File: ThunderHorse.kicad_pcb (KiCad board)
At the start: 2 copper layers, 0 parts

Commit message: Initial layout
Added the components to the board.

TODO:
Review the schematic before continuing the layout.
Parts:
- added BZ1: Buzzer, Custom_Parts:FUET_9018, F.Cu at (226.4, 77.0)
- added C1: 10u, Capacitor_SMD:C_0805_2012Metric, F.Cu at (266.6, 53.8)
- added C10: 10u, Capacitor_SMD:C_0805_2012Metric, F.Cu at (266.6, 62.8)
- added C100: 1u, Capacitor_SMD:C_0603_1608Metric, F.Cu at (263.8, 120.0)
- added C101: 10u, Capacitor_SMD:C_0805_2012Metric, F.Cu at (238.9, 68.2)
- added C11: 10u, Capacitor_SMD:C_0805_2012Metric, F.Cu at (266.6, 65.8)
- added C12: 22u, Capacitor_SMD:C_1206_3216Metric, F.Cu at (261.5, 70.7)
- added C13: 22u, Capacitor_SMD:C_1206_3216Metric, F.Cu at (261.5, 74.0)
- added C14: 10u, Capacitor_SMD:C_0805_2012Metric, F.Cu at (266.6, 68.8)
- added C15: 22u, Capacitor_SMD:C_1206_3216Metric, F.Cu at (261.5, 77.4)
- added C16: 15p, Capacitor_SMD:C_0603_1608Metric, F.Cu at (222.6, 52.9)
- added C17: 100n, Capacitor_SMD:C_0603_1608Metric, F.Cu at (222.6, 55.4)
- added C18: 10u, Capacitor_SMD:C_0805_2012Metric, F.Cu at (238.9, 53.2)
- added C19: 100n, Capacitor_SMD:C_0603_1608Metric, F.Cu at (222.6, 57.9)
- added C2: 10u, Capacitor_SMD:C_0805_2012Metric, F.Cu at (266.6, 56.8)
- added C20: 15p, Capacitor_SMD:C_0603_1608Metric, F.Cu at (222.6, 60.5)
- added C21: 100n, Capacitor_SMD:C_0603_1608Metric, F.Cu at (222.6, 63.0)
- added C22: 100n, Capacitor_SMD:C_0603_1608Metric, F.Cu at (222.6, 65.5)
- added C23: 100n, Capacitor_SMD:C_0603_1608Metric, F.Cu at (222.6, 68.0)
- added C24: 100n, Capacitor_SMD:C_0603_1608Metric, F.Cu at (222.6, 70.5)
- added C25: 100n, Capacitor_SMD:C_0603_1608Metric, F.Cu at (226.6, 52.9)
- added C26: 10u, Capacitor_SMD:C_0805_2012Metric, F.Cu at (238.9, 56.2)
- added C27: 100n, Capacitor_SMD:C_0603_1608Metric, F.Cu at (226.6, 55.4)
- added C28: 100n, Capacitor_SMD:C_0603_1608Metric, F.Cu at (226.6, 57.9)
- added C29: 100n, Capacitor_SMD:C_0603_1608Metric, F.Cu at (226.6, 60.5)
- added C3: 10u, Capacitor_SMD:C_0805_2012Metric, F.Cu at (266.6, 59.8)
- added C30: 10u, Capacitor_SMD:C_0805_2012Metric, F.Cu at (238.9, 59.2)
- added C31: 100n, Capacitor_SMD:C_0603_1608Metric, F.Cu at (226.6, 63.0)
- added C32: 100n, Capacitor_SMD:C_0603_1608Metric, F.Cu at (226.6, 65.5)
- added C33: 10u, Capacitor_SMD:C_0805_2012Metric, F.Cu at (238.9, 62.2)
- added C34: 100n, Capacitor_SMD:C_0805_2012Metric, F.Cu at (238.9, 65.2)
- added C35: 1u, Capacitor_SMD:C_0603_1608Metric, F.Cu at (174.4, 18.5)
- added C36: 10u, Capacitor_SMD:C_1206_3216Metric, F.Cu at (187.2, 18.9)
- added C37: 100n, Capacitor_SMD:C_0603_1608Metric, F.Cu at (174.4, 21.0)
- added C38: 10u, Capacitor_SMD:C_1206_3216Metric, F.Cu at (187.2, 22.2)
- added C39: 10u, Capacitor_SMD:C_1206_3216Metric, F.Cu at (187.2, 25.6)
- added C4: 22u, Capacitor_SMD:C_1206_3216Metric, F.Cu at (261.5, 54.0)
- added C40: 10u, Capacitor_SMD:C_1206_3216Metric, F.Cu at (187.2, 28.9)
- added C41: 10u, Capacitor_SMD:C_1206_3216Metric, F.Cu at (187.2, 32.3)
- added C42: 10u, Capacitor_SMD:C_0805_2012Metric, F.Cu at (192.3, 31.3)
- added C43: 1u, Capacitor_SMD:C_0603_1608Metric, F.Cu at (174.4, 23.5)
- added C44: 1u, Capacitor_SMD:C_0603_1608Metric, F.Cu at (174.4, 26.0)
- added C45: 1u, Capacitor_SMD:C_0603_1608Metric, F.Cu at (174.4, 28.5)
- added C46: 1u, Capacitor_SMD:C_0603_1608Metric, F.Cu at (202.3, 18.5)
- added C47: 10u, Capacitor_SMD:C_1206_3216Metric, F.Cu at (215.2, 18.9)
- added C48: 100n, Capacitor_SMD:C_0603_1608Metric, F.Cu at (202.3, 21.0)
- added C49: 10u, Capacitor_SMD:C_1206_3216Metric, F.Cu at (215.2, 22.2)
- added C5: 100n, Capacitor_SMD:C_0603_1608Metric, F.Cu at (270.8, 53.5)
- added C50: 10u, Capacitor_SMD:C_1206_3216Metric, F.Cu at (215.2, 25.6)
- added C51: 10u, Capacitor_SMD:C_1206_3216Metric, F.Cu at (215.2, 28.9)
- added C52: 10u, Capacitor_SMD:C_1206_3216Metric, F.Cu at (215.2, 32.3)
- added C53: 10u, Capacitor_SMD:C_0805_2012Metric, F.Cu at (220.2, 31.3)
- added C54: 1u, Capacitor_SMD:C_0603_1608Metric, F.Cu at (202.3, 23.5)
- added C55: 1u, Capacitor_SMD:C_0603_1608Metric, F.Cu at (202.3, 26.0)
- added C56: 1u, Capacitor_SMD:C_0603_1608Metric, F.Cu at (202.3, 28.5)
- added C57: 1u, Capacitor_SMD:C_0603_1608Metric, F.Cu at (257.8, 18.1)
- added C58: 10u, Capacitor_SMD:C_1206_3216Metric, F.Cu at (270.6, 18.5)
- added C59: 100n, Capacitor_SMD:C_0603_1608Metric, F.Cu at (257.8, 20.6)
- added C6: 22u, Capacitor_SMD:C_1206_3216Metric, F.Cu at (261.5, 57.3)
- added C60: 10u, Capacitor_SMD:C_1206_3216Metric, F.Cu at (270.6, 21.9)
- added C61: 10u, Capacitor_SMD:C_1206_3216Metric, F.Cu at (270.6, 25.2)
- added C62: 10u, Capacitor_SMD:C_1206_3216Metric, F.Cu at (270.6, 28.6)
- added C63: 10u, Capacitor_SMD:C_1206_3216Metric, F.Cu at (270.6, 31.9)
- added C64: 10u, Capacitor_SMD:C_0805_2012Metric, F.Cu at (275.7, 31.0)
- added C65: 1u, Capacitor_SMD:C_0603_1608Metric, F.Cu at (257.8, 23.1)
- added C66: 1u, Capacitor_SMD:C_0603_1608Metric, F.Cu at (257.8, 25.6)
- added C67: 1u, Capacitor_SMD:C_0603_1608Metric, F.Cu at (257.8, 28.1)
- added C68: 1u, Capacitor_SMD:C_0603_1608Metric, F.Cu at (230.2, 18.0)
- added C69: 10u, Capacitor_SMD:C_1206_3216Metric, F.Cu at (243.0, 18.4)
- added C7: 22u, Capacitor_SMD:C_1206_3216Metric, F.Cu at (261.5, 60.6)
- added C70: 100n, Capacitor_SMD:C_0603_1608Metric, F.Cu at (230.2, 20.5)
- added C71: 10u, Capacitor_SMD:C_1206_3216Metric, F.Cu at (243.0, 21.7)
- added C72: 10u, Capacitor_SMD:C_1206_3216Metric, F.Cu at (243.0, 25.1)
- added C73: 10u, Capacitor_SMD:C_1206_3216Metric, F.Cu at (243.0, 28.4)
- added C74: 10u, Capacitor_SMD:C_1206_3216Metric, F.Cu at (243.0, 31.8)
- added C75: 10u, Capacitor_SMD:C_0805_2012Metric, F.Cu at (248.1, 30.8)
- added C76: 1u, Capacitor_SMD:C_0603_1608Metric, F.Cu at (230.2, 23.0)
- added C77: 1u, Capacitor_SMD:C_0603_1608Metric, F.Cu at (230.2, 25.5)
- added C78: 1u, Capacitor_SMD:C_0603_1608Metric, F.Cu at (230.2, 28.0)
- added C79: 10u, Capacitor_SMD:C_0805_2012Metric, F.Cu at (238.4, 93.7)
- added C8: 22u, Capacitor_SMD:C_1206_3216Metric, F.Cu at (261.5, 64.0)
- added C80: 100n, Capacitor_SMD:C_0603_1608Metric, F.Cu at (250.7, 93.5)
- added C81: 10u, Capacitor_SMD:C_0805_2012Metric, F.Cu at (238.4, 96.8)
- added C82: 10u, Capacitor_SMD:C_0805_2012Metric, F.Cu at (238.4, 99.8)
- added C83: 100n, Capacitor_SMD:C_0201_0603Metric, F.Cu at (247.5, 93.1)
- added C84: 100n, Capacitor_SMD:C_0201_0603Metric, F.Cu at (247.5, 94.9)
- added C85: 100n, Capacitor_SMD:C_0201_0603Metric, F.Cu at (247.5, 96.6)
- added C86: 10u, Capacitor_SMD:C_0805_2012Metric, F.Cu at (272.0, 122.8)
- added C87: 10n, Capacitor_SMD:C_0603_1608Metric, F.Cu at (259.8, 112.5)
- added C88: 10n, Capacitor_SMD:C_0603_1608Metric, F.Cu at (259.8, 115.0)
- added C89: 10u, Capacitor_SMD:C_0805_2012Metric, F.Cu at (272.0, 125.8)
- added C9: 22u, Capacitor_SMD:C_1206_3216Metric, F.Cu at (261.5, 67.3)
- added C90: 100n, Capacitor_SMD:C_0603_1608Metric, F.Cu at (259.8, 117.5)
- added C91: 100n, Capacitor_SMD:C_0603_1608Metric, F.Cu at (259.8, 120.0)
- added C92: 100n, Capacitor_SMD:C_0603_1608Metric, F.Cu at (263.8, 112.5)
- added C94: 100p, Capacitor_SMD:C_0603_1608Metric, F.Cu at (263.8, 115.0)
- added C96: 100p, Capacitor_SMD:C_0603_1608Metric, F.Cu at (263.8, 117.5)
- added D1: 1N5819WS, Diode_SMD:D_SOD-323, F.Cu at (266.2, 100.7)
- added D2: WS2812B, Custom_Parts:WS2812B-2020, F.Cu at (234.3, 76.6)
- added D3: LED, LED_SMD:LED_0805_2012Metric, F.Cu at (234.4, 73.3)
- added FL1: LFB182G45SG9B740, Custom_Parts:LFB182G45SG9B740, F.Cu at (266.3, 129.1)
- added H1: M4, Custom_Parts:MOUNTING_FC_4.0mm, B.Cu at (162.0, 74.0)
- added H2: M4, Custom_Parts:MOUNTING_FC_4.0mm, B.Cu at (118.0, 126.0)
- added H3: M4, Custom_Parts:MOUNTING_FC_4.0mm, B.Cu at (162.0, 126.0)
- added H4: M4, Custom_Parts:MOUNTING_FC_4.0mm, B.Cu at (118.0, 74.0)
- added J1: JTAG, Custom_Parts:PAD_5_SQUARE_SOLID_1.0x1.0mm_P1.5mm, F.Cu at (245.3, 52.9)
- added J10: MOTOR2, Custom_Parts:PAD_3_SQUARE_SOLID_2.0x2.0mm_P2.5mm, F.Cu at (205.2, 36.7)
- added J11: SWD3, Custom_Parts:PAD_2_SQUARE_SOLID_1.0x1.0mm_P1.5mm, F.Cu at (257.8, 39.5)
- added J12: MOTOR3, Custom_Parts:PAD_3_SQUARE_SOLID_2.0x2.0mm_P2.5mm, F.Cu at (260.6, 36.3)
- added J13: SWD4, Custom_Parts:PAD_2_SQUARE_SOLID_1.0x1.0mm_P1.5mm, F.Cu at (230.1, 39.4)
- added J14: MOTOR4, Custom_Parts:PAD_3_SQUARE_SOLID_2.0x2.0mm_P2.5mm, F.Cu at (233.0, 36.2)
- added J16: UFL, Connector_Coaxial:U.FL_Hirose_U.FL-R-SMT-1_Vertical, F.Cu at (267.0, 124.3)
- added J2: HH-16P-CB-TYPE-C, Custom_Parts:HH-16P-CB-TYPE-C, F.Cu at (267.6, 90.3)
- added J3: GPS, Custom_Parts:PAD_6_SQUARE_SOLID_1.5x1.5mm_P2.0mm, F.Cu at (227.1, 93.6)
- added J4: CAM, Custom_Parts:PAD_6_SQUARE_SOLID_1.5x1.5mm_P2.0mm, F.Cu at (227.1, 96.7)
- added J5: GPS, Connector_JST:JST_SH_SM06B-SRSS-TB_1x06-1MP_P1.00mm_Horizontal, F.Cu at (226.0, 102.0)
- added J6: CAM, Connector_JST:JST_SH_SM06B-SRSS-TB_1x06-1MP_P1.00mm_Horizontal, F.Cu at (226.0, 109.6)
- added J7: SWD1, Custom_Parts:PAD_2_SQUARE_SOLID_1.0x1.0mm_P1.5mm, F.Cu at (174.3, 39.9)
- added J8: MOTOR1, Custom_Parts:PAD_3_SQUARE_SOLID_2.0x2.0mm_P2.5mm, F.Cu at (177.2, 36.7)
- added J9: SWD2, Custom_Parts:PAD_2_SQUARE_SOLID_1.0x1.0mm_P1.5mm, F.Cu at (202.3, 39.9)
- added L1: 1.5u, Inductor_SMD:L_Panasonic_PCC-M0530M, F.Cu at (273.2, 68.1)
- added L2: B201610S3R3, Custom_Parts:AOTAB201610S3R3101T, F.Cu at (249.4, 62.2)
- added L3: 15u, Inductor_SMD:L_0603_1608Metric, F.Cu at (267.8, 112.5)
- added Q1: SI2301BDS, Package_TO_SOT_SMD:SOT-23, F.Cu at (266.5, 97.0)
- added Q10: XRS306D, Custom_Parts:PDFN8_DUAL_3.3x3.3mm, F.Cu at (279.4, 37.1)
- added Q11: XRS306D, Custom_Parts:PDFN8_DUAL_3.3x3.3mm, F.Cu at (242.5, 37.0)
- added Q12: XRS306D, Custom_Parts:PDFN8_DUAL_3.3x3.3mm, F.Cu at (247.2, 37.0)
- added Q13: XRS306D, Custom_Parts:PDFN8_DUAL_3.3x3.3mm, F.Cu at (251.8, 37.0)
- added Q14: SI2312BDS, Package_TO_SOT_SMD:SOT-23, F.Cu at (249.2, 65.9)
- added Q2: XRS306D, Custom_Parts:PDFN8_DUAL_3.3x3.3mm, F.Cu at (186.7, 37.5)
- added Q3: XRS306D, Custom_Parts:PDFN8_DUAL_3.3x3.3mm, F.Cu at (191.4, 37.5)
- added Q4: XRS306D, Custom_Parts:PDFN8_DUAL_3.3x3.3mm, F.Cu at (196.0, 37.5)
- added Q5: XRS306D, Custom_Parts:PDFN8_DUAL_3.3x3.3mm, F.Cu at (214.7, 37.5)
- added Q6: XRS306D, Custom_Parts:PDFN8_DUAL_3.3x3.3mm, F.Cu at (219.3, 37.5)
- added Q7: XRS306D, Custom_Parts:PDFN8_DUAL_3.3x3.3mm, F.Cu at (224.0, 37.5)
- added Q8: XRS306D, Custom_Parts:PDFN8_DUAL_3.3x3.3mm, F.Cu at (270.1, 37.1)
- added Q9: XRS306D, Custom_Parts:PDFN8_DUAL_3.3x3.3mm, F.Cu at (274.8, 37.1)
- added R1: 10K, Resistor_SMD:R_0603_1608Metric, F.Cu at (270.8, 56.0)
- added R10: 27, Resistor_SMD:R_0603_1608Metric, F.Cu at (230.6, 60.5)
- added R11: 27, Resistor_SMD:R_0603_1608Metric, F.Cu at (230.6, 63.0)
- added R12: 1K, Resistor_SMD:R_0603_1608Metric, F.Cu at (230.6, 65.5)
- added R13: 5.1K, Resistor_SMD:R_0603_1608Metric, F.Cu at (230.6, 68.0)
- added R14: 5.1K, Resistor_SMD:R_0603_1608Metric, F.Cu at (230.6, 70.5)
- added R15: 10K, Resistor_SMD:R_0603_1608Metric, F.Cu at (234.6, 52.9)
- added R16: 5.1K, Resistor_SMD:R_0603_1608Metric, F.Cu at (262.1, 96.1)
- added R17: 5.1K, Resistor_SMD:R_0603_1608Metric, F.Cu at (262.1, 98.6)
- added R18: 10K, Resistor_SMD:R_0603_1608Metric, F.Cu at (262.1, 101.1)
- added R19: 10K, Resistor_SMD:R_0603_1608Metric, F.Cu at (174.4, 31.0)
- added R2: 680K, Resistor_SMD:R_0603_1608Metric, F.Cu at (270.8, 58.5)
- added R20: 10K, Resistor_SMD:R_0603_1608Metric, F.Cu at (174.4, 33.5)
- added R21: 2.2K, Resistor_SMD:R_0603_1608Metric, F.Cu at (178.4, 18.5)
- added R22: 10K, Resistor_SMD:R_0603_1608Metric, F.Cu at (178.4, 21.0)
- added R23: 1K, Resistor_SMD:R_0603_1608Metric, F.Cu at (178.4, 23.5)
- added R24: 10K, Resistor_SMD:R_0603_1608Metric, F.Cu at (178.4, 26.0)
- added R25: 2.2K, Resistor_SMD:R_0603_1608Metric, F.Cu at (178.4, 28.5)
- added R26: 10K, Resistor_SMD:R_0603_1608Metric, F.Cu at (178.4, 31.0)
- added R27: 10K, Resistor_SMD:R_0603_1608Metric, F.Cu at (178.4, 33.5)
- added R28: 2.2K, Resistor_SMD:R_0603_1608Metric, F.Cu at (182.4, 18.5)
- added R29: 10, Resistor_SMD:R_0603_1608Metric, F.Cu at (182.4, 21.0)
- added R3: 130K, Resistor_SMD:R_0603_1608Metric, F.Cu at (270.8, 61.1)
- added R30: 10, Resistor_SMD:R_0603_1608Metric, F.Cu at (182.4, 23.5)
- added R31: 10, Resistor_SMD:R_0603_1608Metric, F.Cu at (182.4, 26.0)
- added R32: 10, Resistor_SMD:R_0603_1608Metric, F.Cu at (182.4, 28.5)
- added R33: 10, Resistor_SMD:R_0603_1608Metric, F.Cu at (182.4, 31.0)
- added R34: 10, Resistor_SMD:R_0603_1608Metric, F.Cu at (182.4, 33.5)
- added R35: 10K, Resistor_SMD:R_0603_1608Metric, F.Cu at (202.3, 31.0)
- added R36: 10K, Resistor_SMD:R_0603_1608Metric, F.Cu at (202.3, 33.5)
- added R37: 2.2K, Resistor_SMD:R_0603_1608Metric, F.Cu at (206.3, 18.5)
- added R38: 10K, Resistor_SMD:R_0603_1608Metric, F.Cu at (206.3, 21.0)
- added R39: 1K, Resistor_SMD:R_0603_1608Metric, F.Cu at (206.3, 23.5)
- added R4: 100K, Resistor_SMD:R_0603_1608Metric, F.Cu at (270.8, 63.6)
- added R40: 10K, Resistor_SMD:R_0603_1608Metric, F.Cu at (206.3, 26.0)
- added R41: 2.2K, Resistor_SMD:R_0603_1608Metric, F.Cu at (206.3, 28.5)
- added R42: 10K, Resistor_SMD:R_0603_1608Metric, F.Cu at (206.3, 31.0)
- added R43: 10K, Resistor_SMD:R_0603_1608Metric, F.Cu at (206.3, 33.5)
- added R44: 2.2K, Resistor_SMD:R_0603_1608Metric, F.Cu at (210.4, 18.5)
- added R45: 10, Resistor_SMD:R_0603_1608Metric, F.Cu at (210.4, 21.0)
- added R46: 10, Resistor_SMD:R_0603_1608Metric, F.Cu at (210.4, 23.5)
- added R47: 10, Resistor_SMD:R_0603_1608Metric, F.Cu at (210.4, 26.0)
- added R48: 10, Resistor_SMD:R_0603_1608Metric, F.Cu at (210.4, 28.5)
- added R49: 10, Resistor_SMD:R_0603_1608Metric, F.Cu at (210.4, 31.0)
- added R5: 1K, Resistor_SMD:R_0603_1608Metric, F.Cu at (226.6, 68.0)
- added R50: 10, Resistor_SMD:R_0603_1608Metric, F.Cu at (210.4, 33.5)
- added R51: 10K, Resistor_SMD:R_0603_1608Metric, F.Cu at (257.8, 30.6)
- added R52: 10K, Resistor_SMD:R_0603_1608Metric, F.Cu at (257.8, 33.2)
- added R53: 2.2K, Resistor_SMD:R_0603_1608Metric, F.Cu at (261.8, 18.1)
- added R54: 10K, Resistor_SMD:R_0603_1608Metric, F.Cu at (261.8, 20.6)
- added R55: 1K, Resistor_SMD:R_0603_1608Metric, F.Cu at (261.8, 23.1)
- added R56: 10K, Resistor_SMD:R_0603_1608Metric, F.Cu at (261.8, 25.6)
- added R57: 2.2K, Resistor_SMD:R_0603_1608Metric, F.Cu at (261.8, 28.1)
- added R58: 10K, Resistor_SMD:R_0603_1608Metric, F.Cu at (261.8, 30.6)
- added R59: 10K, Resistor_SMD:R_0603_1608Metric, F.Cu at (261.8, 33.2)
- added R6: 10K, Resistor_SMD:R_0603_1608Metric, F.Cu at (226.6, 70.5)
- added R60: 2.2K, Resistor_SMD:R_0603_1608Metric, F.Cu at (265.8, 18.1)
- added R61: 10, Resistor_SMD:R_0603_1608Metric, F.Cu at (265.8, 20.6)
- added R62: 10, Resistor_SMD:R_0603_1608Metric, F.Cu at (265.8, 23.1)
- added R63: 10, Resistor_SMD:R_0603_1608Metric, F.Cu at (265.8, 25.6)
- added R64: 10, Resistor_SMD:R_0603_1608Metric, F.Cu at (265.8, 28.1)
- added R65: 10, Resistor_SMD:R_0603_1608Metric, F.Cu at (265.8, 30.6)
- added R66: 10, Resistor_SMD:R_0603_1608Metric, F.Cu at (265.8, 33.2)
- added R67: 10K, Resistor_SMD:R_0603_1608Metric, F.Cu at (230.2, 30.5)
- added R68: 10K, Resistor_SMD:R_0603_1608Metric, F.Cu at (230.2, 33.0)
- added R69: 2.2K, Resistor_SMD:R_0603_1608Metric, F.Cu at (234.2, 18.0)
- added R7: 100K, Resistor_SMD:R_0603_1608Metric, F.Cu at (230.6, 52.9)
- added R70: 10K, Resistor_SMD:R_0603_1608Metric, F.Cu at (234.2, 20.5)
- added R71: 1K, Resistor_SMD:R_0603_1608Metric, F.Cu at (234.2, 23.0)
- added R72: 10K, Resistor_SMD:R_0603_1608Metric, F.Cu at (234.2, 25.5)
- added R73: 2.2K, Resistor_SMD:R_0603_1608Metric, F.Cu at (234.2, 28.0)
- added R74: 10K, Resistor_SMD:R_0603_1608Metric, F.Cu at (234.2, 30.5)
- added R75: 10K, Resistor_SMD:R_0603_1608Metric, F.Cu at (234.2, 33.0)
- added R76: 2.2K, Resistor_SMD:R_0603_1608Metric, F.Cu at (238.2, 18.0)
- added R77: 10, Resistor_SMD:R_0603_1608Metric, F.Cu at (238.2, 20.5)
- added R78: 10, Resistor_SMD:R_0603_1608Metric, F.Cu at (238.2, 23.0)
- added R79: 10, Resistor_SMD:R_0603_1608Metric, F.Cu at (238.2, 25.5)
- added R8: 10K, Resistor_SMD:R_0603_1608Metric, F.Cu at (230.6, 55.4)
- added R80: 10, Resistor_SMD:R_0603_1608Metric, F.Cu at (238.2, 28.0)
- added R81: 10, Resistor_SMD:R_0603_1608Metric, F.Cu at (238.2, 30.5)
- added R82: 10, Resistor_SMD:R_0603_1608Metric, F.Cu at (238.2, 33.0)
- added R83: 10K, Resistor_SMD:R_0603_1608Metric, F.Cu at (250.7, 96.0)
- added R84: R002, Resistor_SMD:R_2512_6332Metric, F.Cu at (245.0, 100.0)
- added R85: 10K, Resistor_SMD:R_0603_1608Metric, F.Cu at (267.8, 115.0)
- added R86: 100K, Resistor_SMD:R_0603_1608Metric, F.Cu at (267.8, 117.5)
- added R87: 100K, Resistor_SMD:R_0603_1608Metric, F.Cu at (267.8, 120.0)
- added R88: 1K, Resistor_SMD:R_0603_1608Metric, F.Cu at (234.6, 55.4)
- added R89: 100, Resistor_SMD:R_0603_1608Metric, F.Cu at (234.6, 57.9)
- added R9: 27, Resistor_SMD:R_0603_1608Metric, F.Cu at (230.6, 57.9)
- added R90: 100K, Resistor_SMD:R_0603_1608Metric, F.Cu at (234.6, 60.5)
- added SW1: TS2306A, Custom_Parts:SW_SMD_3.0x2.0_PUSH, F.Cu at (243.9, 62.3)
- added SW2: TS2306A, Custom_Parts:SW_SMD_3.0x2.0_PUSH, F.Cu at (243.9, 65.5)
- added U1: 21700_DUAL_HOLDER, Custom_Parts:21700_DUAL_HOLDER_MOUNTING, B.Cu at (140.0, 100.0)
- added U10: DRV8300D, Custom_Parts:VQFN-24-1EP_4x4mm_P0.5mm_EP2.45x2.45mm, F.Cu at (221.2, 26.7)
- added U11: STM32G071GBUxN, Custom_Parts:QFN-28_4x4mm_P0.5mm, F.Cu at (277.0, 20.0)
- added U12: DRV8300D, Custom_Parts:VQFN-24-1EP_4x4mm_P0.5mm_EP2.45x2.45mm, F.Cu at (276.6, 26.3)
- added U13: STM32G071GBUxN, Custom_Parts:QFN-28_4x4mm_P0.5mm, F.Cu at (249.4, 19.9)
- added U14: DRV8300D, Custom_Parts:VQFN-24-1EP_4x4mm_P0.5mm_EP2.45x2.45mm, F.Cu at (249.0, 26.2)
- added U15: TPRT9013-33, Package_TO_SOT_SMD:SOT-23-5, F.Cu at (248.2, 104.9)
- added U16: ICM-42688-P, Custom_Parts:ICM-42688-P, F.Cu at (243.1, 104.8)
- added U17: BMP280, Package_LGA:Bosch_LGA-8_2x2.5mm_P0.65mm_ClockwisePinNumbering, F.Cu at (238.4, 103.3)
- added U18: INA230, Package_DFN_QFN:VQFN-16-1EP_3x3mm_P0.5mm_EP1.6x1.6mm_ThermalVias, F.Cu at (243.6, 94.9)
- added U19: TPRT9013-33, Package_TO_SOT_SMD:SOT-23-5, F.Cu at (272.4, 118.9)
- added U2: TPS63070RNMR, Custom_Parts:TPS63070RNMR, F.Cu at (275.5, 54.8)
- added U20: SX1280IMLTRT, Package_DFN_QFN:QFN-24-1EP_4x4mm_P0.5mm_EP2.6x2.6mm_ThermalVias, F.Cu at (261.3, 124.4)
- added U21: AT2401C, Package_DFN_QFN:QFN-16-1EP_3x3mm_P0.5mm_EP1.7x1.7mm_ThermalVias, F.Cu at (272.9, 113.9)
- added U3: TPRT9013-33, Package_TO_SOT_SMD:SOT-23-5, F.Cu at (271.4, 73.8)
- added U4: RP2354B, Custom_Parts:RP2350B_QFN-80_EP_10.573x10.573_Pitch0.4mm, F.Cu at (243.1, 76.2)
- added U5: W25Q128JVPIQ, Package_SON:WSON-8-1EP_6x5mm_P1.27mm_EP3.4x4.3mm, F.Cu at (245.3, 57.4)
- added U6: TPD2E001DRLR, Package_TO_SOT_SMD:SOT-553, F.Cu at (270.7, 96.5)
- added U7: STM32G071GBUxN, Custom_Parts:QFN-28_4x4mm_P0.5mm, F.Cu at (193.6, 20.4)
- added U8: DRV8300D, Custom_Parts:VQFN-24-1EP_4x4mm_P0.5mm_EP2.45x2.45mm, F.Cu at (193.2, 26.7)
- added U9: STM32G071GBUxN, Custom_Parts:QFN-28_4x4mm_P0.5mm, F.Cu at (221.5, 20.4)
- added Y1: 40MHz, Crystal:Crystal_SMD_2016-4Pin_2.0x1.6mm, F.Cu at (234.2, 80.2)
- added Y2: 52MHz/10ppm, Crystal:Crystal_SMD_2016-4Pin_2.0x1.6mm, F.Cu at (271.8, 129.1)
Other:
- board outline added: 120 x 60 mm

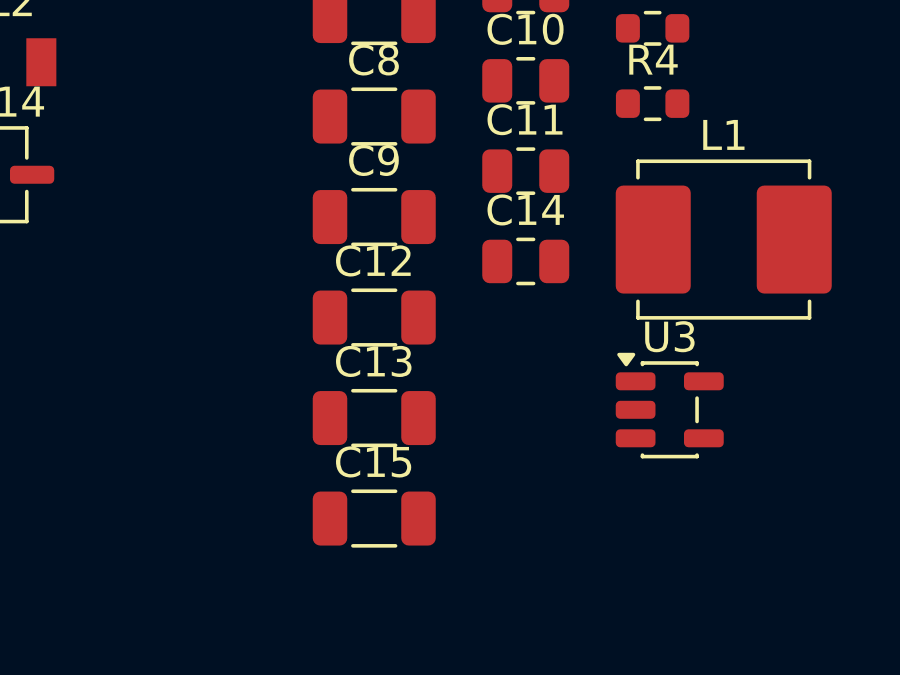
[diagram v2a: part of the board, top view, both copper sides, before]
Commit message: Net nodes
Added the missing net nodes in the schematic.
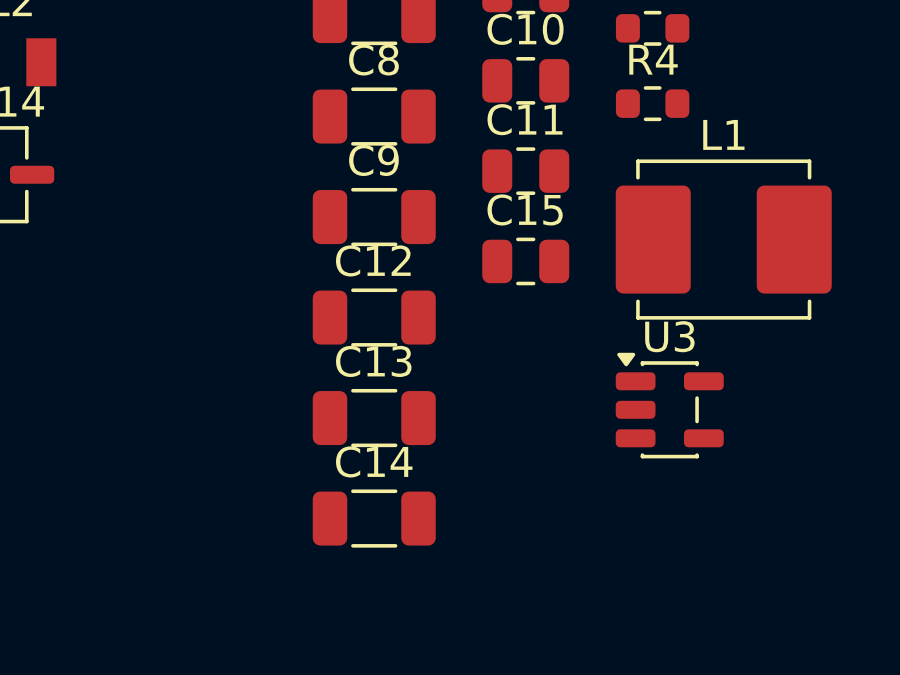
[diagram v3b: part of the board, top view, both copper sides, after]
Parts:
- renumbered C15 to C14, C14 to C15
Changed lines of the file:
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@@
 		(descr "Capacitor SMD 0805 (2012 Metric), square (rectangular) end terminal, IPC-7351 nominal, (Body size source: IPC-SM-782 page 76, https://www.pcb-3d.com/wordpress/wp-content/uploads/ipc-sm-782a_amendment_1_and_2.pdf, https://docs.google.com/spreadsheets/d/1BsfQQcO9C6DZCsRaXUlFlo91Tg2WpOkGARC1WS5S8t0/edit?usp=sharing), generated with kicad-footprint-generator")
 		(tags "capacitor")
-		(property "Reference" "C14"
+		(property "Reference" "C15"
 			(at 0 -1.68 0)
 			(layer "F.SilkS")
@@
 		(descr "Capacitor SMD 1206 (3216 Metric), square (rectangular) end terminal, IPC-7351 nominal, (Body size source: IPC-SM-782 page 76, https://www.pcb-3d.com/wordpress/wp-content/uploads/ipc-sm-782a_amendment_1_and_2.pdf), generated with kicad-footprint-generator")
 		(tags "capacitor")
-		(property "Reference" "C15"
+		(property "Reference" "C14"
 			(at 0 -1.85 0)
 			(layer "F.SilkS")

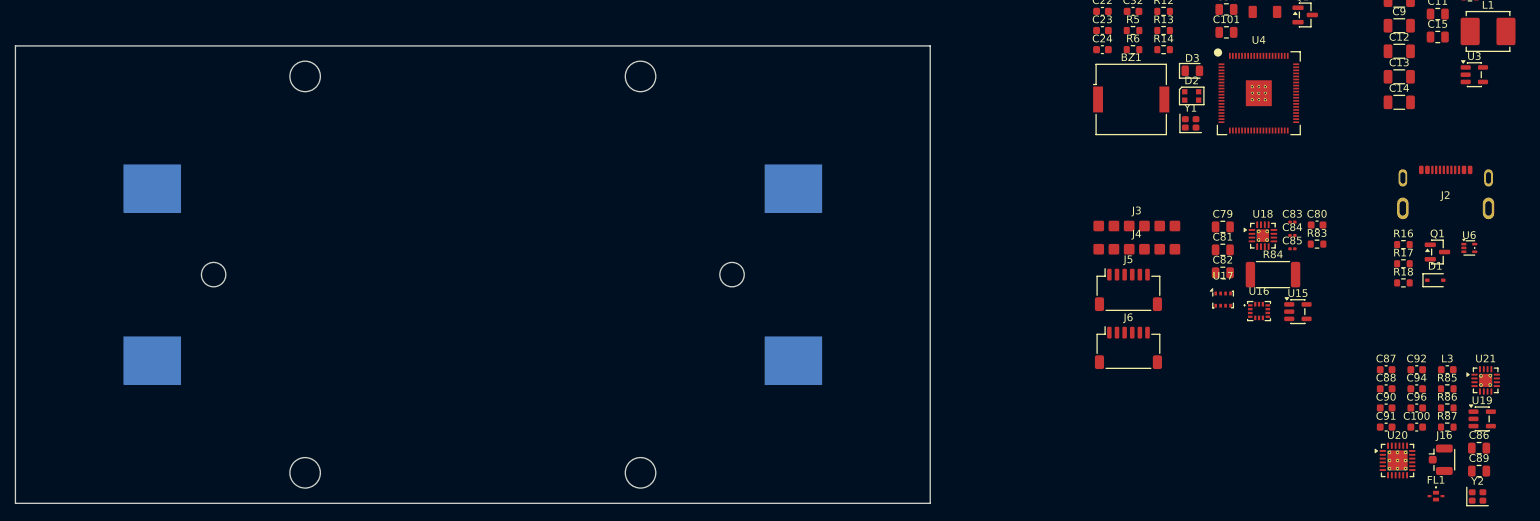
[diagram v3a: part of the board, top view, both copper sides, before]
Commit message: Net nodes and layout
Updated all net nodes definitions.
Updated the board layout.

TODO:
Define the net dimensions for the layout.
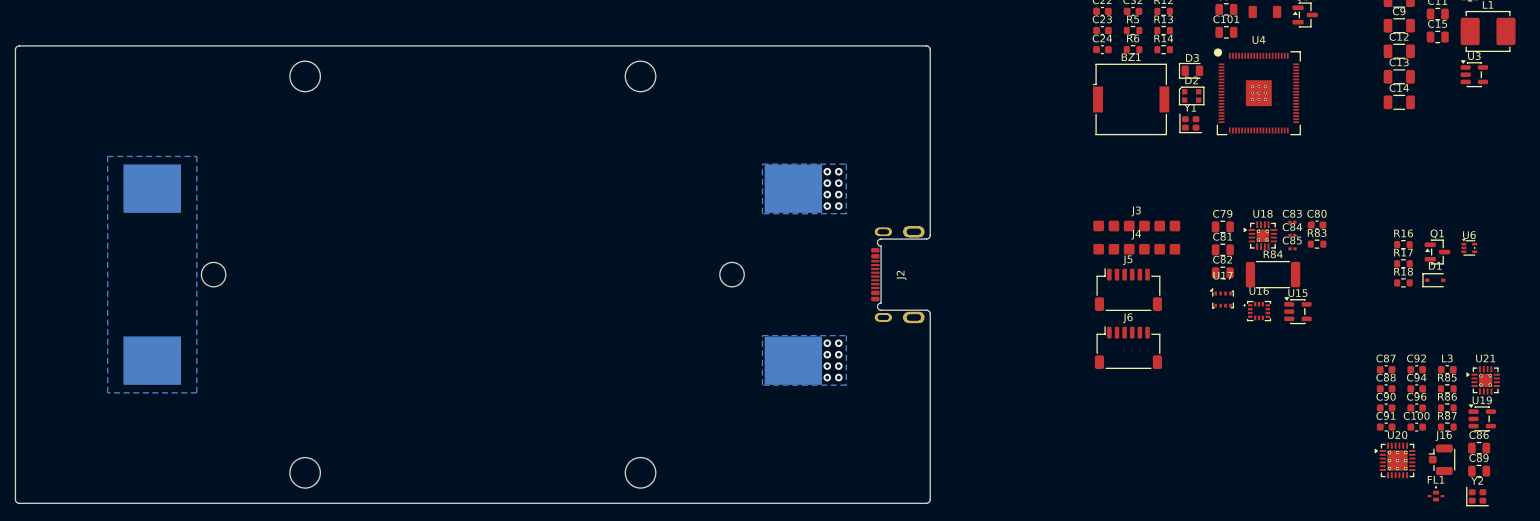
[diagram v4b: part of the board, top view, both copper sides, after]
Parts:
- J2: value HH-16P-CB-TYPE-C -> USB4510031A
- moved J2 71.5 mm to (196.8, 100.0), turned to 90 degrees
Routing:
- net VBAT_IN: vias 0 -> 8
- net GND: vias 0 -> 8
- added copper zone on B.Cu, net /Power/BAT_JUMP
- added copper zone on In2.Cu, net 5V
- added copper zone on B.Cu, net GND
- added copper zone on In1.Cu, net GND
- added copper zone on In4.Cu, net GND
- added copper zone on In3.Cu, net VBAT
- added copper zone on B.Cu, net VBAT_IN
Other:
- outline, holes or cut-outs redrawn
- copper layers 2 -> 6

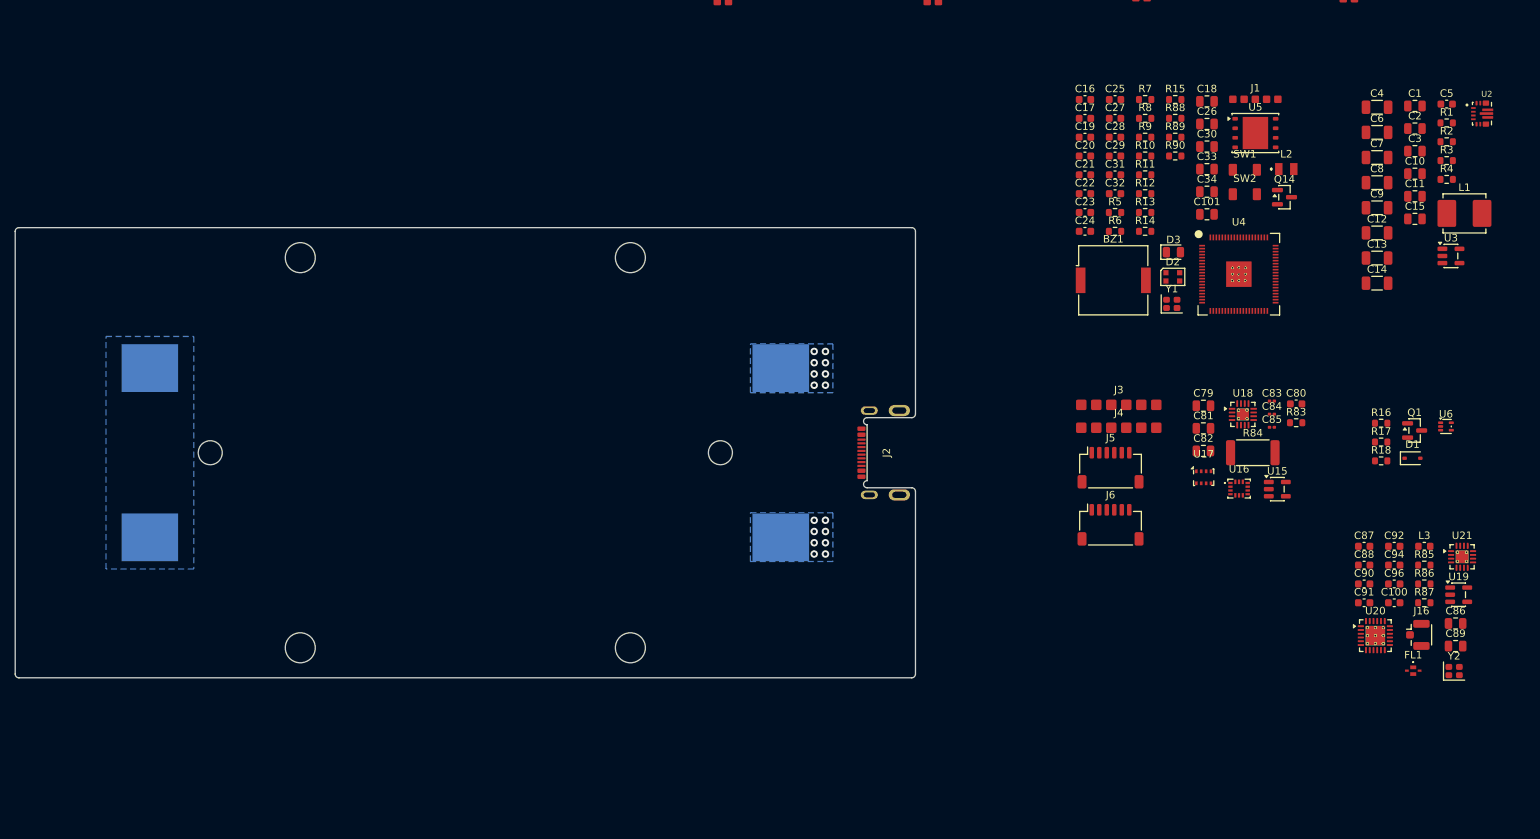
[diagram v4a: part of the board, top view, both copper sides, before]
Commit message: Board outline and net nodes
Added an initial board outline.
Updated net nodes definitions.
Updated board rules for manufacturing.
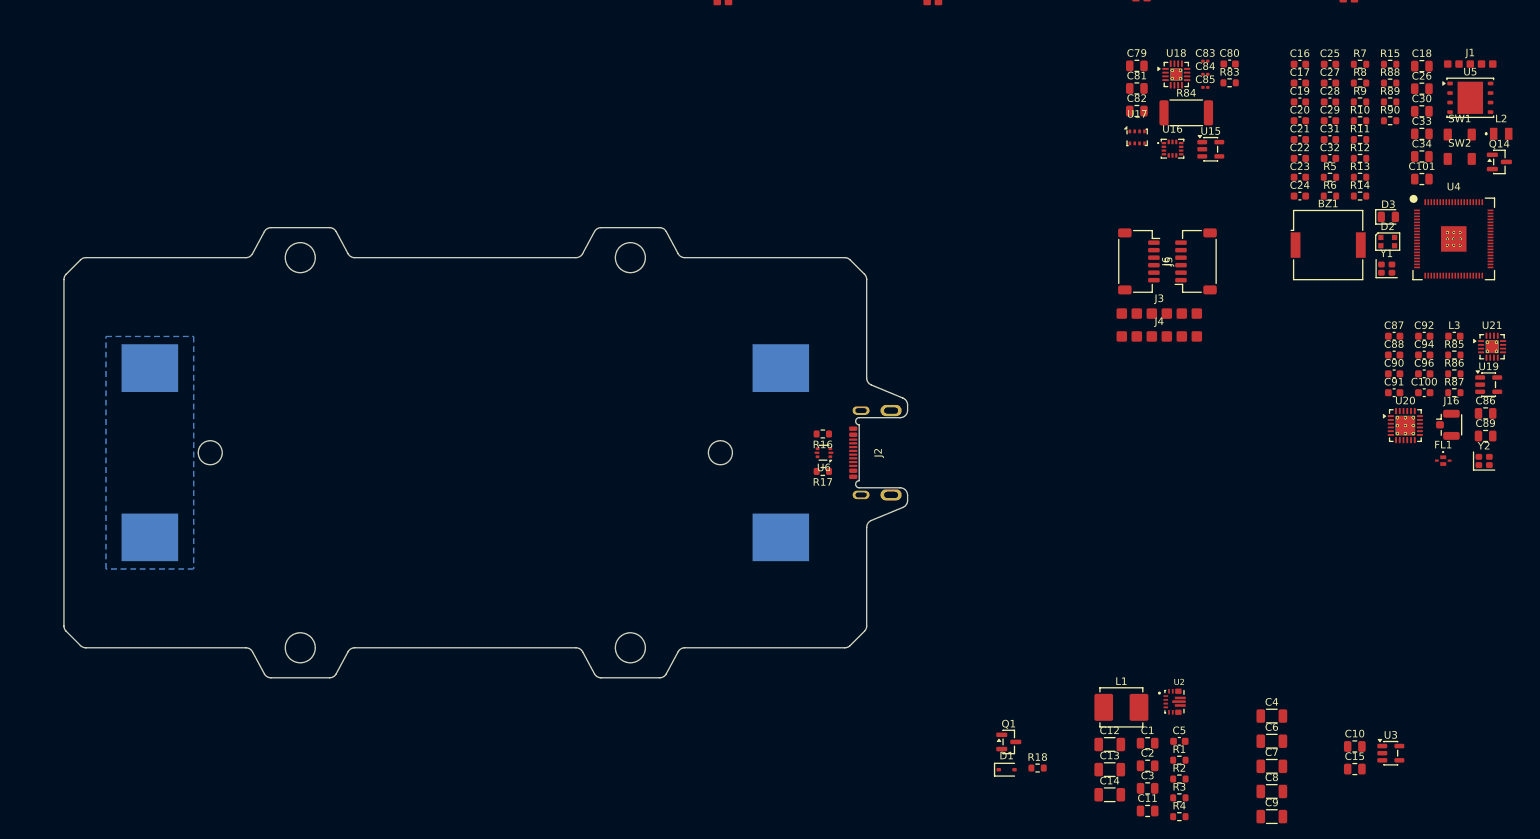
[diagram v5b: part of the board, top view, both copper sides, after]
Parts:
- J2: value USB4510031A -> HH-16P-CB-TYPE-C
- U18: footprint Package_DFN_QFN:VQFN-16-1EP_3x3mm_P0.5mm_EP1.6x1.6mm_ThermalVias -> Custom_Parts:VQFN-16-1EP_3x3mm_P0.5mm_EP1.6x1.6mm_ThermalVias
- U6: value TPD2E001DRLR -> USBLC6-2P6; footprint Package_TO_SOT_SMD:SOT-553 -> Package_TO_SOT_SMD:SOT-666
- moved C3 92.1 mm to (230.9, 144.7)
- moved R2 92.1 mm to (235.2, 143.5)
- moved C1 92.1 mm to (230.9, 138.7)
- moved C2 92.1 mm to (230.9, 141.7)
- moved C5 92.1 mm to (235.2, 138.5)
- moved R1 92.1 mm to (235.2, 141.0)
- moved R3 92.1 mm to (235.2, 146.0)
- moved R4 92.1 mm to (235.2, 148.5)
- moved C11 89.3 mm to (230.9, 147.8)
- moved U2 88.5 mm to (234.5, 133.2)
- moved U6 83.0 mm to (187.8, 100.0), turned to 180 degrees
- moved C7 82.4 mm to (247.5, 141.8)
- moved C8 82.4 mm to (247.5, 145.2)
- moved C9 82.4 mm to (247.5, 148.5)
- moved C4 82.4 mm to (247.5, 135.1)
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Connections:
- R10 pad 2: /MCU/USBC_D- -> /MCU/USBT_D-
- R9 pad 2: /MCU/USBC_D+ -> /MCU/USBT_D+
- U6 pad 1: /MCU/VBUS -> /MCU/USBC_D-
- U6 pad 2: unconnected-(U6-NC-Pad2) -> GND
- U6 pad 3: /MCU/USBC_D- -> /MCU/USBC_D+
- U6 pad 4: GND -> /MCU/USBT_D+
- U6 pad 5: /MCU/USBC_D+ -> /MCU/VBUS
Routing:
- net VBAT_IN: vias 8 -> 0
- net GND: vias 8 -> 0
- removed copper zone on B.Cu, net GND
- removed copper zone on B.Cu, net VBAT_IN
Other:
- board size 120 x 60 mm -> 112.5 x 60 mm
